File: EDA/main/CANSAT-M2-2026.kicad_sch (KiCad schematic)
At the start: 44 parts, among them J4 STM32H7_SWD, J6 SKRPACE010, U7 STM32H7S3L8H6, Y2 25MHz, Y3 ABS07-32.768KHZ-T

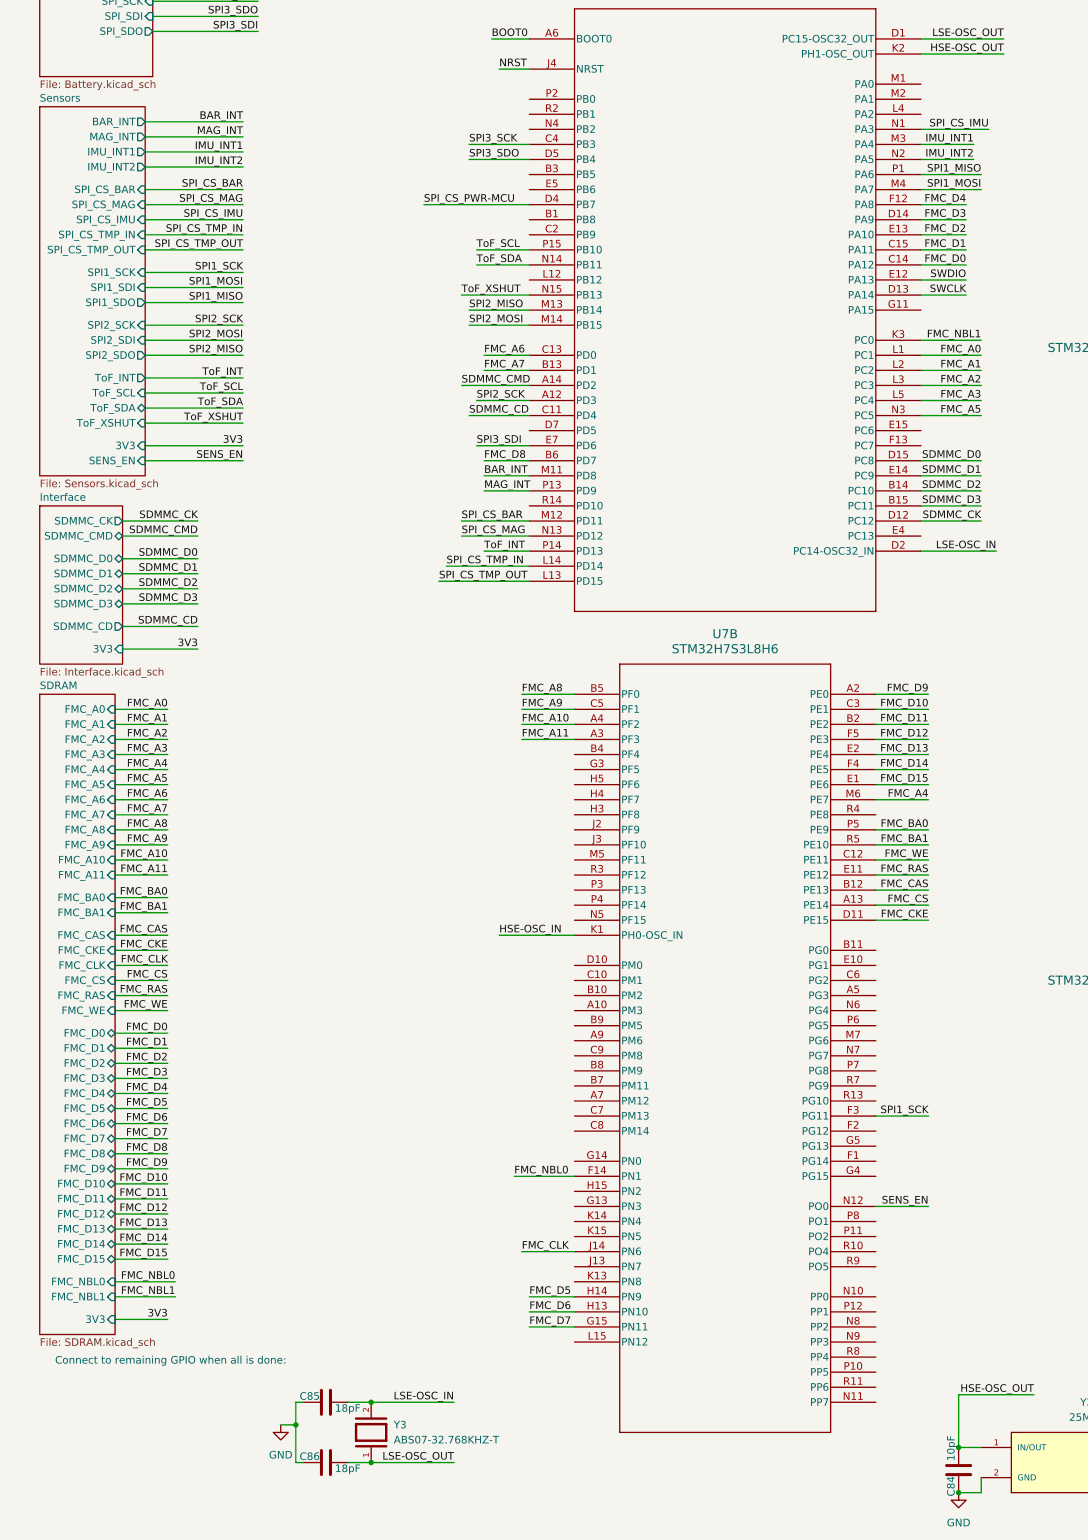
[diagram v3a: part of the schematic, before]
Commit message: Finished gas sensor PCB, and added connector for it on main PCB
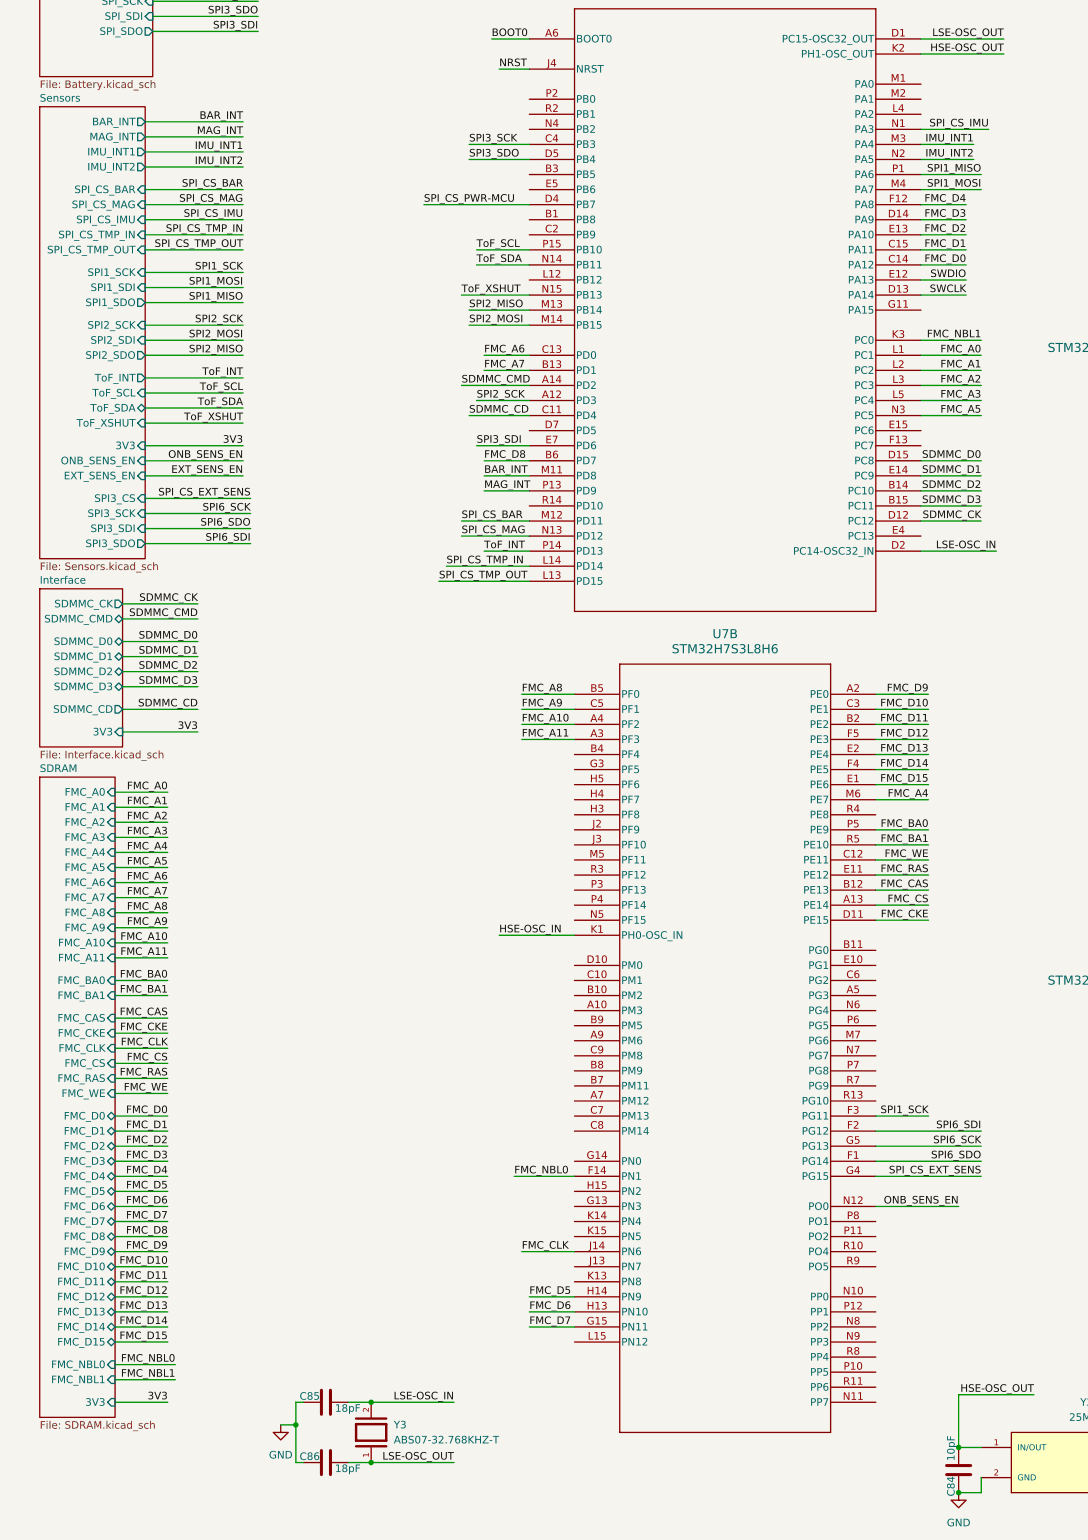
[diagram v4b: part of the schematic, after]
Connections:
- net SPI6_SDO: now reaches U7.F1 (PG14)
- net SPI6_SDI: now reaches U7.F2 (PG12)
- net SPI_CS_EXT_SENS: now reaches U7.G4 (PG15)
- net SPI6_SCK: now reaches U7.G5 (PG13)
- net SENS_EN renamed ONB_SENS_EN
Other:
- sheet Sensors ports: added EXT_SENS_EN, ONB_SENS_EN, SPI3_CS, SPI3_SCK, SPI3_SDI, SPI3_SDO; removed SENS_EN
- note removed: "Connect to remaining GPIO when all is done:"

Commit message: Added GNSS and SIM800L
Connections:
- net SPI3_SDI: now also U7.D5 (PB4); no longer U7.E7 (PD6)
- net SPI3_SDO: now also U7.B3 (PB5); no longer U7.D5 (PB4)
- net MCU<GNSS_RX: now reaches U7.R3 (PF12)
- net MCU>SIM_TX: now reaches U7.D7 (PD5)
- net 5V_EN: now reaches U7.E4 (PC13)
- net MCU>GNSS_TX: now reaches U7.E5 (PB6)
- new net MCU<SIM_RX: U7.E7 (PD6)
- no-connect marks 7 -> 9
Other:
- sheet Interface ports: added 5V, GNSS_EN, GNSS_PPS, GNSS_RST, GNSS_RX, GNSS_SCL, GNSS_SDA, GNSS_TX, SIM_RST, SIM_RX, SIM_TX; removed none
- sheet Power ports: added 5V, 5V_EN; removed none
- note added: "I2C for the GNSS module is not being used, as it is slower and clunkier than UART"

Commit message: Uploaded work
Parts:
- FB1: footprint (none) -> Inductor_SMD:L_0603_1608Metric
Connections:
- net GND: no longer C51.2, C52.2, C53.2, C54.2, C55.2, C56.2, C57.2, C58.2, C59.2, C60.1, C62.1, C63.1, C64.1, C65.1, C7.2, C71.2, C72.2, C73.2, C74.2, C75.2, C76.2, C77.1, C78.1, FB1.1, J4.1, J6.2, U7.D9 (VDD50USB), U7.F10 (VDD), U7.F7 (VDD), U7.F8 (VDD33USB), U7.F9 (VDD), U7.G6 (VDD), U7.G7 (VDDLDO), U7.G9 (VDDLDO), U7.H10 (VDD), U7.H12 (VDDXSPI2), U7.H6 (VDD), U7.J11 (VDDXSPI2), U7.J7 (VDDLDO), U7.J9 (VDDLDO), U7.K10 (VDD), U7.K12 (VDDXSPI2), U7.K6 (VDD), U7.K8 (VDD), U7.L10 (VDDXSPI1), U7.L8 (VDDXSPI1), U7.L9 (VDD), U7.M10 (VDDXSPI1)
- net 3V3: now reaches C61.2, C70.2, U7.C1 (VBAT), U7.D8 (DVDD)
- net 3V3: now also C51.2, C52.2, C53.2, C54.2, C55.2, C56.2, C57.2, C58.2, C59.2, C60.1, C62.1, C63.1, C64.1, C65.1, C7.2, C71.2, C72.2, C73.2, C74.2, C75.2, C76.2, C77.1, C78.1, FB1.1, J4.1, J6.2, U7.D9 (VDD50USB), U7.F10 (VDD), U7.F7 (VDD), U7.F8 (VDD33USB), U7.F9 (VDD), U7.G6 (VDD), U7.G7 (VDDLDO), U7.G9 (VDDLDO), U7.H10 (VDD), U7.H12 (VDDXSPI2), U7.H6 (VDD), U7.J11 (VDDXSPI2), U7.J7 (VDDLDO), U7.J9 (VDDLDO), U7.K10 (VDD), U7.K12 (VDDXSPI2), U7.K6 (VDD), U7.K8 (VDD), U7.L10 (VDDXSPI1), U7.L8 (VDDXSPI1), U7.L9 (VDD), U7.M10 (VDDXSPI1)
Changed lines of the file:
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@@
 	)
 	(junction
-		(at 242.57 200.66)
+		(at 250.19 30.48)
 		(diameter 0)
 		(color 0 0 0 0)
 	)
 	(junction
-		(at 242.57 149.86)
+		(at 242.57 200.66)
 		(diameter 0)
 		(color 0 0 0 0)
 	)
 	(junction
-		(at 242.57 215.9)
+		(at 242.57 149.86)
 		(diameter 0)
 		(color 0 0 0 0)
 	)
 	(junction
-		(at 250.19 22.86)
+		(at 242.57 215.9)
 		(diameter 0)
 		(color 0 0 0 0)
@@
 	(wire
 		(pts
-			(xy 260.35 22.86) (xy 250.19 22.86)
-		)
-		(stroke
-			(width 0)
-			(type default)
-		)
-	)
-	(wire
-		(pts
 			(xy 240.03 90.17) (xy 276.86 90.17)
 		)
@@
 	(wire
 		(pts
+			(xy 250.19 30.48) (xy 265.43 30.48)
+		)
+		(stroke
+			(width 0)
+			(type default)
+		)
+	)
+	(wire
+		(pts
 			(xy 212.09 270.51) (xy 215.9 270.51)
 		)
@@
 	)
 	(label "CORE_3V3"
-		(at 260.35 22.86 180)
+		(at 265.43 30.48 180)
 		(effects
 			(font
@@
 			)
 		)
-		(property "Footprint" ""
+		(property "Footprint" "Inductor_SMD:L_0603_1608Metric"
 			(at 264.16 108.712 90)
 			(effects

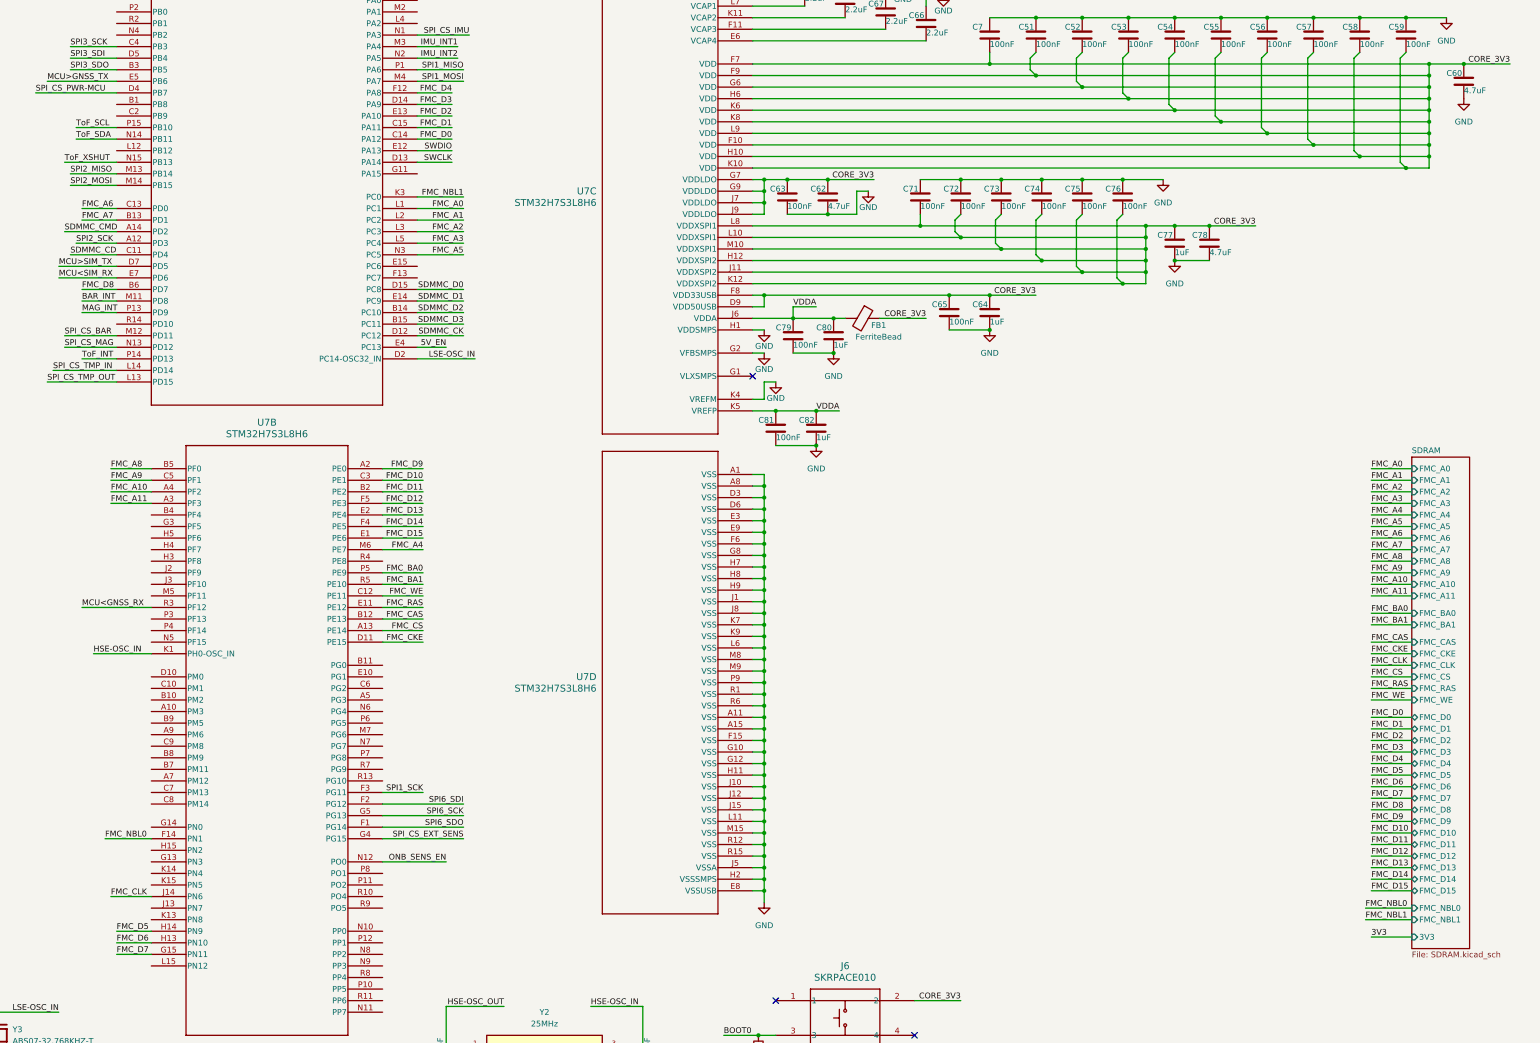
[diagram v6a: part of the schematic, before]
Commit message: Made main branch not include SDRAM
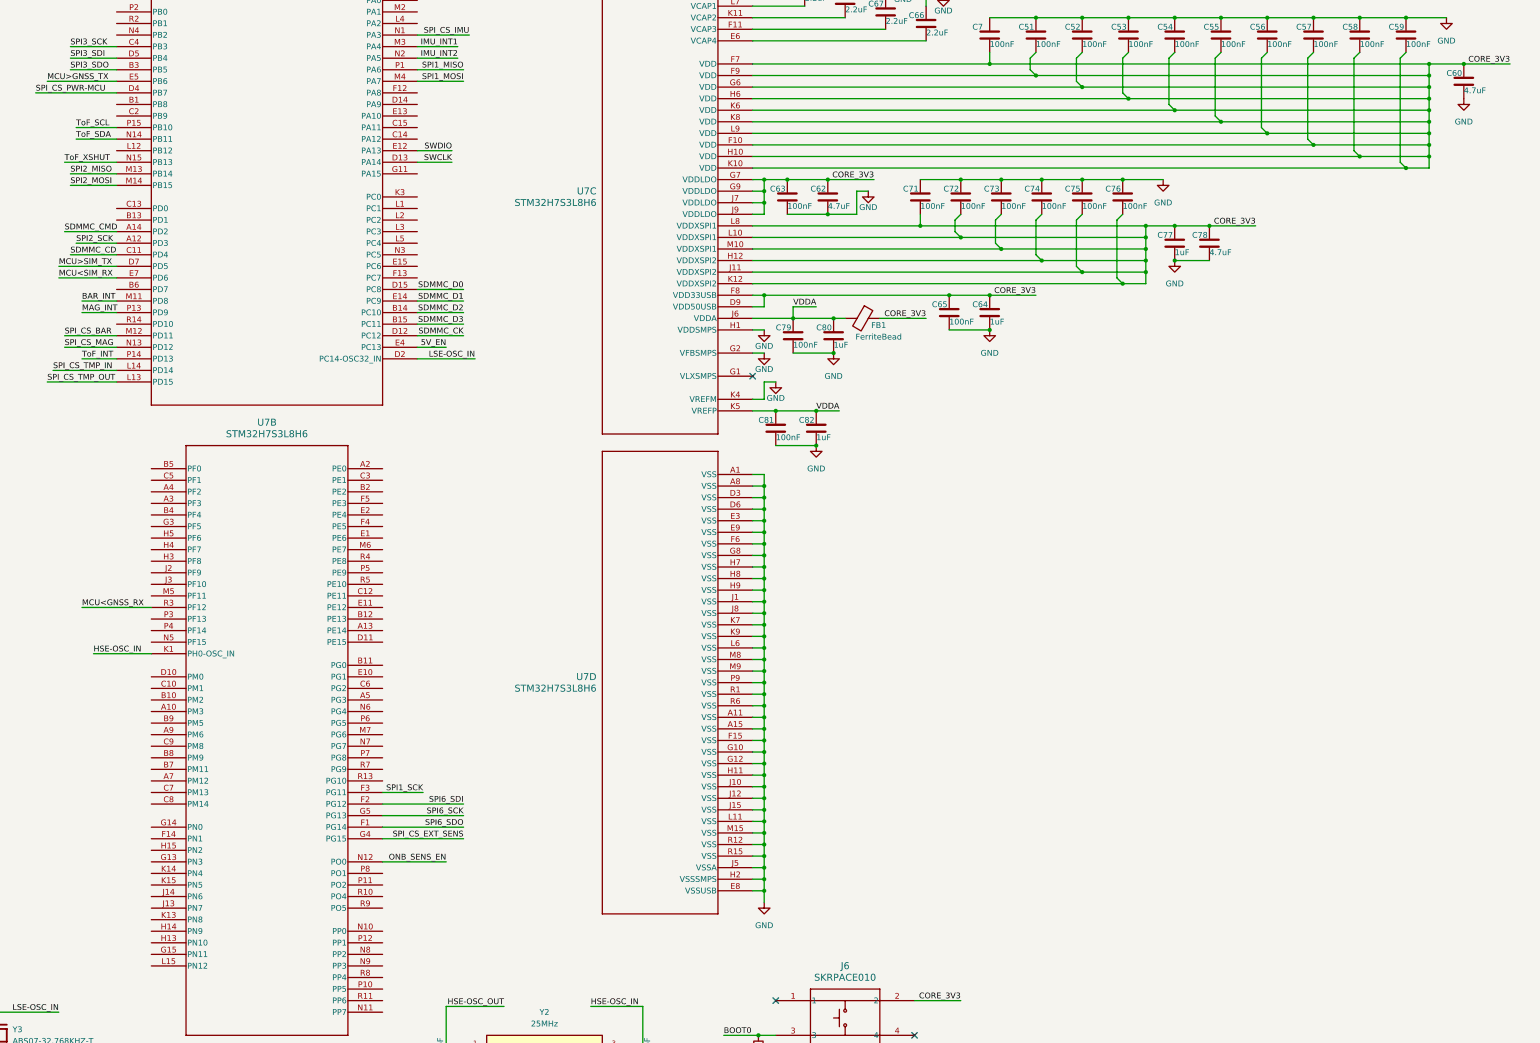
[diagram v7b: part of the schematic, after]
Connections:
- net FMC_A0: no longer names the net of U7.L1 (PC1)
- net FMC_A1: no longer names the net of U7.L2 (PC2)
- net FMC_A10: no longer names the net of U7.A4 (PF2)
- net FMC_A11: no longer names the net of U7.A3 (PF3)
- net FMC_A2: no longer names the net of U7.L3 (PC3)
- net FMC_A3: no longer names the net of U7.L5 (PC4)
- net FMC_A4: no longer names the net of U7.M6 (PE7)
- net FMC_A5: no longer names the net of U7.N3 (PC5)
- net FMC_A6: no longer names the net of U7.C13 (PD0)
- net FMC_A7: no longer names the net of U7.B13 (PD1)
- net FMC_A8: no longer names the net of U7.B5 (PF0)
- net FMC_A9: no longer names the net of U7.C5 (PF1)
- net FMC_BA0: no longer names the net of U7.P5 (PE9)
- net FMC_BA1: no longer names the net of U7.R5 (PE10)
- net FMC_CAS: no longer names the net of U7.B12 (PE13)
- net FMC_CKE: no longer names the net of U7.D11 (PE15)
- net FMC_CLK: no longer names the net of U7.J14 (PN6)
- net FMC_CS: no longer names the net of U7.A13 (PE14)
- net FMC_D0: no longer names the net of U7.C14 (PA12)
- net FMC_D1: no longer names the net of U7.C15 (PA11)
- net FMC_D10: no longer names the net of U7.C3 (PE1)
- net FMC_D11: no longer names the net of U7.B2 (PE2)
- net FMC_D12: no longer names the net of U7.F5 (PE3)
- net FMC_D13: no longer names the net of U7.E2 (PE4)
- net FMC_D14: no longer names the net of U7.F4 (PE5)
- net FMC_D15: no longer names the net of U7.E1 (PE6)
- net FMC_D2: no longer names the net of U7.E13 (PA10)
- net FMC_D3: no longer names the net of U7.D14 (PA9)
- net FMC_D4: no longer names the net of U7.F12 (PA8)
- net FMC_D5: no longer names the net of U7.H14 (PN9)
- net FMC_D6: no longer names the net of U7.H13 (PN10)
- net FMC_D7: no longer names the net of U7.G15 (PN11)
- net FMC_D8: no longer names the net of U7.B6 (PD7)
- net FMC_D9: no longer names the net of U7.A2 (PE0)
- net FMC_NBL0: no longer names the net of U7.F14 (PN1)
- net FMC_NBL1: no longer names the net of U7.K3 (PC0)
- net FMC_RAS: no longer names the net of U7.E11 (PE12)
- net FMC_WE: no longer names the net of U7.C12 (PE11)
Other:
- removed sheet SDRAM

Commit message: Uploaded work
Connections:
- net GNSS_PPS: now also U7.R2 (PB1)
- net USB-DM: now reaches U7.A7 (PM12)
- net USB-DP: now reaches U7.B7 (PM11)
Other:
- sheet Interface ports: added USB-DM, USB-DP; removed none
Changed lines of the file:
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@@
 	(wire
 		(pts
+			(xy 31.75 184.15) (xy 40.64 184.15)
+		)
+		(stroke
+			(width 0)
+			(type default)
+		)
+	)
+	(wire
+		(pts
+			(xy 90.17 45.72) (xy 100.33 45.72)
+		)
+		(stroke
+			(width 0)
+			(type default)
+		)
+	)
+	(wire
+		(pts
 			(xy 383.54 52.07) (xy 382.27 53.34)
 		)
@@
 	(wire
 		(pts
+			(xy 99.06 209.55) (xy 107.95 209.55)
+		)
+		(stroke
+			(width 0)
+			(type default)
+		)
+	)
+	(wire
+		(pts
 			(xy 242.57 218.44) (xy 242.57 220.98)
 		)
@@
 	(wire
 		(pts
+			(xy 31.75 186.69) (xy 40.64 186.69)
+		)
+		(stroke
+			(width 0)
+			(type default)
+		)
+	)
+	(wire
+		(pts
 			(xy 69.85 262.89) (xy 73.66 262.89)
 		)
@@
 	(wire
 		(pts
+			(xy 99.06 212.09) (xy 107.95 212.09)
+		)
+		(stroke
+			(width 0)
+			(type default)
+		)
+	)
+	(wire
+		(pts
 			(xy 87.63 101.6) (xy 100.33 101.6)
 		)
@@
 		)
 	)
+	(label "USB-DM"
+		(at 99.06 212.09 0)
+		(effects
+			(font
+				(size 1.27 1.27)
+			)
+			(justify left bottom)
+		)
+	)
 	(label "SPI2_MISO"
 		(at 52.07 86.36 180)
@@
 		)
 	)
+	(label "USB-DP"
+		(at 99.06 209.55 0)
+		(effects
+			(font
+				(size 1.27 1.27)
+			)
+			(justify left bottom)
+		)
+	)
 	(label "ToF_SDA"
 		(at 91.44 71.12 0)
@@
 		)
 	)
+	(label "USB-DM"
+		(at 40.64 184.15 180)
+		(effects
+			(font
+				(size 1.27 1.27)
+			)
+			(justify right bottom)
+		)
+	)
 	(label "SPI1_MISO"
 		(at 52.07 77.47 180)
@@
 		)
 	)
+	(label "GNSS_PPS"
+		(at 90.17 45.72 0)
+		(effects
+			(font
+				(size 1.27 1.27)
+			)
+			(justify left bottom)
+		)
+	)
 	(label "GNSS_EN"
 		(at 46.99 153.67 180)
@@
 		)
 	)
+	(label "USB-DP"
+		(at 40.64 186.69 180)
+		(effects
+			(font
+				(size 1.27 1.27)
+			)
+			(justify right bottom)
+		)
+	)
 	(label "SDMMC_CMD"
 		(at 88.9 91.44 0)
@@
 	(sheet
 		(at 17.78 125.73)
-		(size 13.97 57.15)
+		(size 13.97 63.5)
 		(exclude_from_sim no)
 		(in_bom yes)
@@
 		)
 		(property "Sheetfile" "Interface.kicad_sch"
-			(at 17.78 183.4646 0)
+			(at 17.78 189.8146 0)
 			(effects
 				(font
@@
 			(effects
 				(font
+					(size 1.27 1.27)
+				)
+				(justify right)
+			)
+		)
+		(pin "USB-DM" bidirectional
+			(at 31.75 184.15 0)
+			(effects
+				(font
+					(size 1.27 1.27)
+				)
+				(justify right)
+			)
+		)
+		(pin "USB-DP" bidirectional
+			(at 31.75 186.69 0)
+			(effects
+				(font
